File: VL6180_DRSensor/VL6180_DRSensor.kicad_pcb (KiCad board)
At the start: 2 copper layers, 19.5 x 20 mm, 21 parts, among them CN4 A1251WR-S-2P, CN5 A1251WR-S-4P, CN6 A1251WR-S-4P, Q1 BL8558-28PRN, Q2 2N7002_C916396, Q3 2N7002_C916396, Q4 2N7002_C916396, U1 1N5819W_C5451628, U2 VL6180V1NR/1

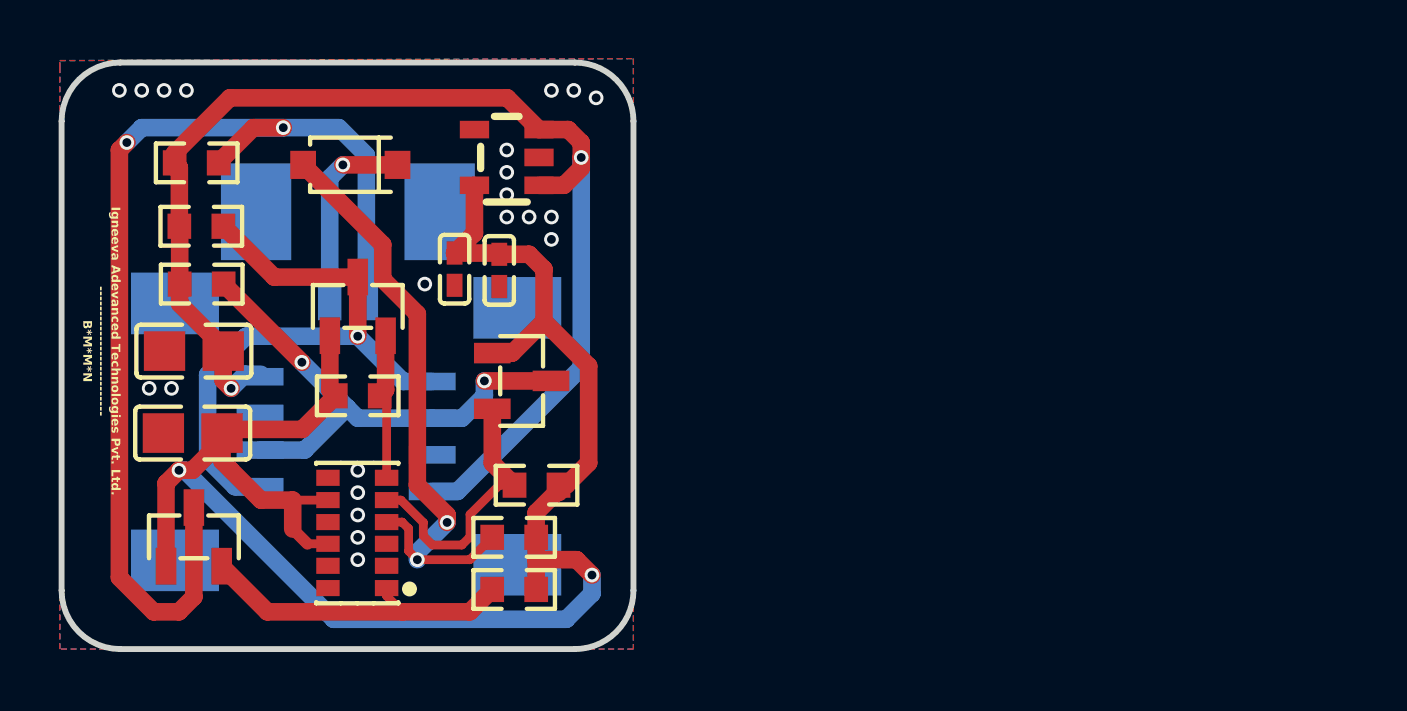
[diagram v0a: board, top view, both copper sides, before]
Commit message: Update Verison
- Screw Hole mounting version with the JST 1.25mm connectors with length tuning
- Size of the PCB is exact size as available in the market
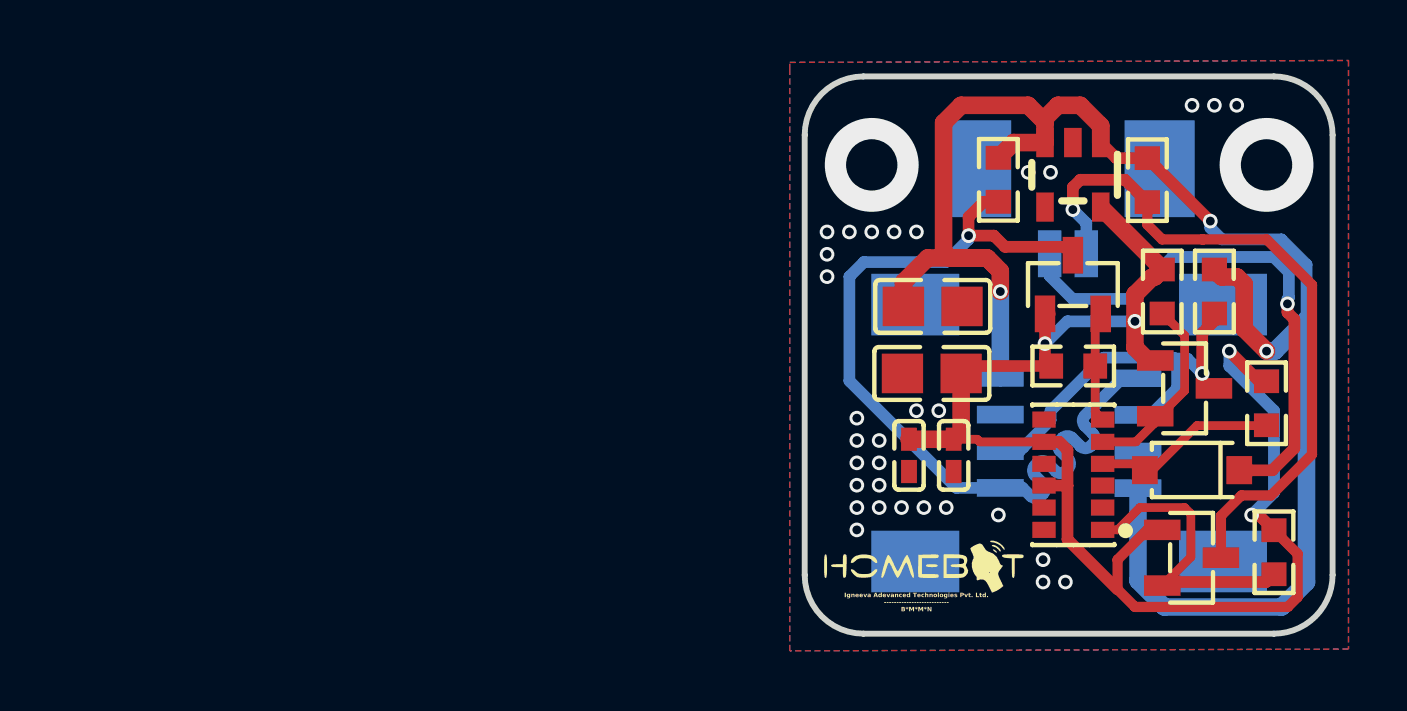
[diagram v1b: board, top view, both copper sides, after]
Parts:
- G***: moved to F.Cu
- moved R2 34.5 mm to (209.3, 71.9), turned to -90 degrees
- moved Q4 34.0 mm to (208.5, 81.0), turned to 180 degrees
- moved R3 32.4 mm to (207.0, 68.1), turned to -90 degrees
- moved U1 30.5 mm to (208.5, 78.0)
- moved R4 27.2 mm to (201.9, 68.1), turned to -90 degrees
- moved R1 26.1 mm to (211.1, 75.7), turned to -90 degrees
- moved R7 25.9 mm to (211.3, 80.8), turned to -90 degrees
- moved C2 25.3 mm to (199.7, 74.7)
- moved CN5 25.2 mm to (200.5, 76.7)
- moved C1 25.2 mm to (199.7, 72.4), turned to 0 degrees
- moved CN4 24.6 mm to (204.3, 69.1)
- moved U2 24.5 mm to (204.5, 78.1)
- moved R5 24.4 mm to (204.5, 74.4)
- moved Q2 24.4 mm to (204.5, 71.6)
- moved CN6 24.1 mm to (208.1, 76.7)
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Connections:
- C1 pad 2: GND -> (no net)
- C2 pad 2: GND -> (no net)
- C3 pad 2: GND -> (no net)
- C4 pad 2: GND -> (no net)
- CN5 pad 2: GND -> (no net)
- CN6 pad 2: GND -> (no net)
- Q1 pad 2: GND -> (no net)
- U2 pad 12: GND -> (no net)
- U2 pad 9: GND -> (no net)
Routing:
- net VCC: track 42.3 -> 59.1 mm, vias 2 -> 3
- net Net-(U1-A): track 20.8 -> 6.32 mm, vias 2 -> 0
- net INT: track 37.5 -> 23.9 mm, vias 2 -> 1
- net CE: track 6.55 -> 18.1 mm
- net SDA: track 21.2 -> 30.8 mm
- net 2.8V: track 59.3 -> 51.1 mm, vias 2 -> 4
- net SCL: track 17.5 -> 14.5 mm, vias 2 -> 1
- net SCL_2.8V: track 9.47 -> 6.60 mm
- net SDA_2.8V: track 5.02 -> 3.79 mm
- net INT_2.8V: track 11.2 -> 10.4 mm
- net GND: vias 22 -> 31
- net (no net): vias 0 -> 2
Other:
- board size 19.5 x 20 mm -> 18 x 19 mm
